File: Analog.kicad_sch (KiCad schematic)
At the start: 25 parts, among them Q2 2N7002, U3 74HC4051, U4 74HC4051, U5 OPA350, U6 MAX5423

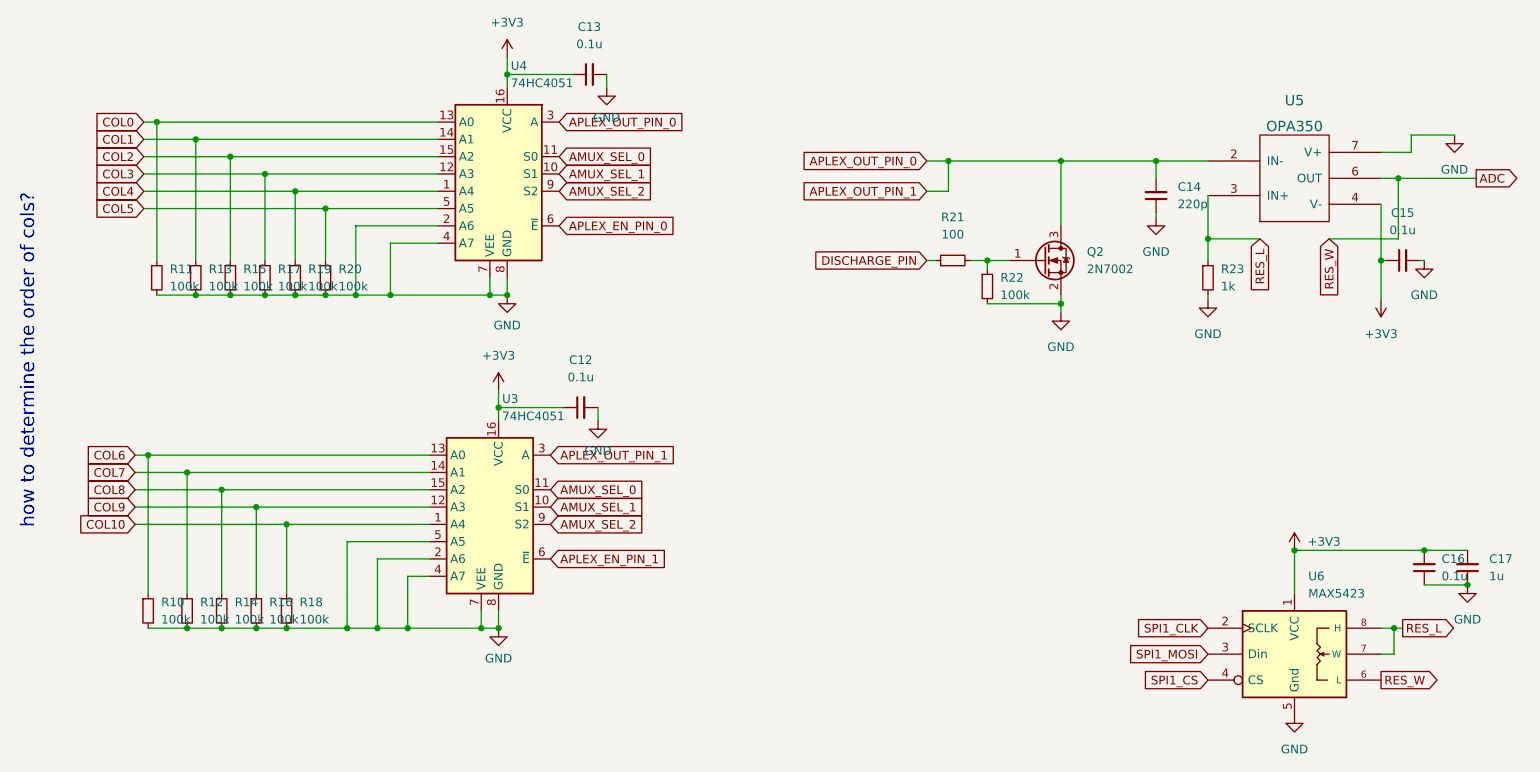
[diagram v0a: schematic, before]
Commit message: component placement
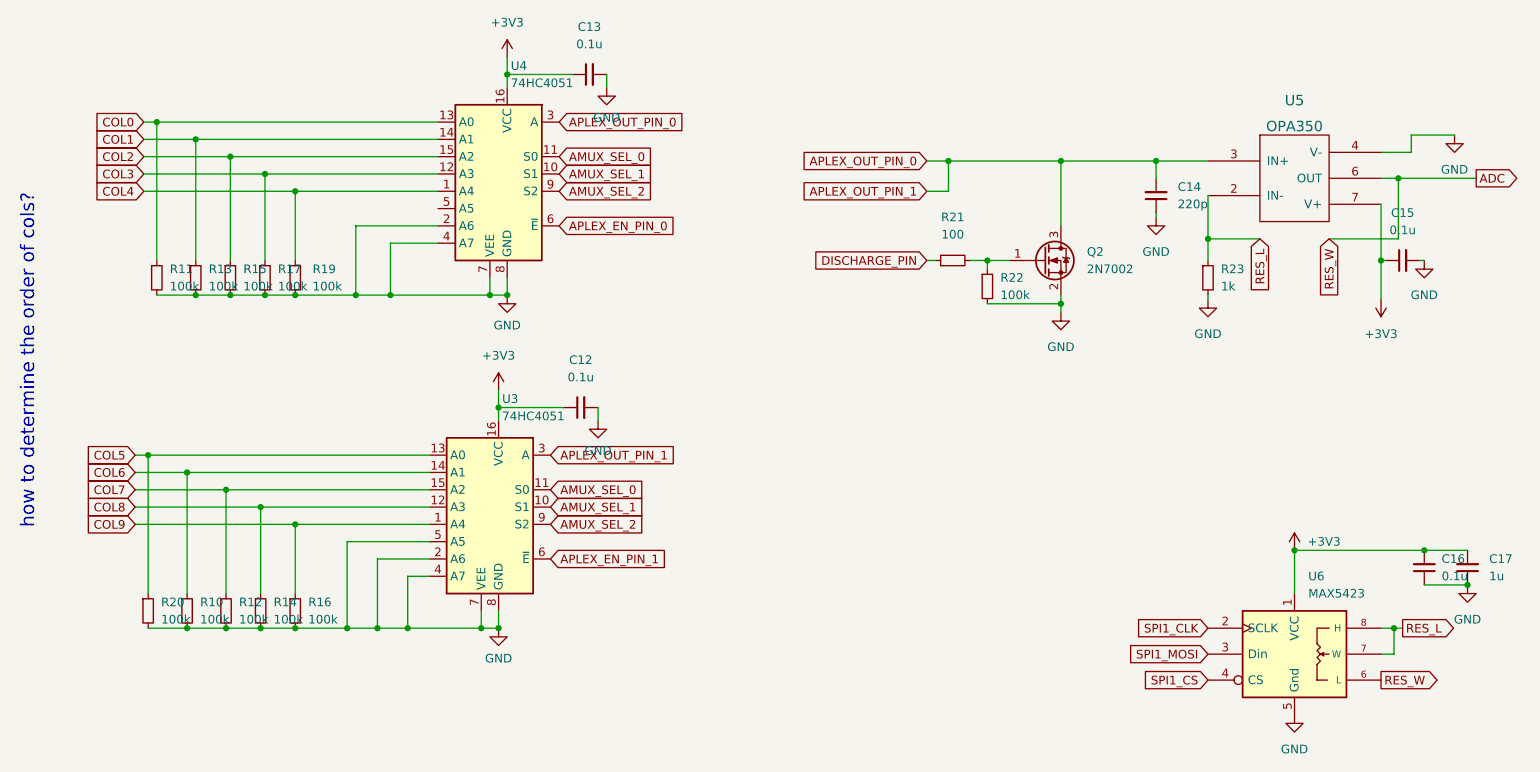
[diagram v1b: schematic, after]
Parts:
- removed R18: 100k, Resistor_SMD:R_0402_1005Metric, symbol Device:R_Small
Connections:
- net COL10 is gone; now on net COL9: U3.1 (A4)
- net +3V3: now also U5.7 (V+); no longer U5.4 (V-)
- net APLEX_OUT_PIN_0: now also U5.3 (IN+); no longer U5.2 (IN-)
- net COL5: now also U3.13 (A0); no longer U4.5 (A5)
- net COL6: now also U3.14 (A1); no longer U3.13 (A0)
- net COL7: now also U3.15 (A2); no longer U3.14 (A1)
- net COL8: now also U3.12 (A3); no longer U3.15 (A2)
- net COL9: no longer U3.12 (A3)
- net GND: now also U5.4 (V-); no longer U5.7 (V+)
- net RES_L: now also U5.2 (IN-); no longer U5.3 (IN+)
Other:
- moved on the sheet: R10, R12, R14, R16, R20

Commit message: routing work
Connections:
- net COL0: now also R15.1, U4.15 (A2); no longer R11.1, U4.13 (A0)
- net COL2: now also R11.1, U4.13 (A0); no longer R15.1, U4.15 (A2)
- net COL5: now also R12.1, U3.15 (A2); no longer R20.1, U3.13 (A0)
- net COL7: now also R20.1, U3.13 (A0); no longer R12.1, U3.15 (A2)
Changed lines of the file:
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@@
     )
   )
-  (global_label "COL2" (shape input) (at 67.945 47.625 180) (fields_autoplaced)
+  (global_label "COL2" (shape input) (at 67.945 42.545 180) (fields_autoplaced)
     (effects (font (size 1.27 1.27)) (justify right))
-    (property "Intersheet References" "${INTERSHEET_REFS}" (id 0) (at 60.6938 47.7044 0)
+    (property "Intersheet References" "${INTERSHEET_REFS}" (id 0) (at 60.6938 42.6244 0)
       (effects (font (size 1.27 1.27)) (justify right) hide)
     )
@@
     )
   )
-  (global_label "COL7" (shape input) (at 66.675 96.52 180) (fields_autoplaced)
+  (global_label "COL7" (shape input) (at 66.675 91.44 180) (fields_autoplaced)
     (effects (font (size 1.27 1.27)) (justify right))
-    (property "Intersheet References" "${INTERSHEET_REFS}" (id 0) (at 59.4238 96.5994 0)
+    (property "Intersheet References" "${INTERSHEET_REFS}" (id 0) (at 59.4238 91.5194 0)
       (effects (font (size 1.27 1.27)) (justify right) hide)
     )
@@
     )
   )
-  (global_label "COL0" (shape input) (at 67.945 42.545 180) (fields_autoplaced)
+  (global_label "COL0" (shape input) (at 67.945 47.625 180) (fields_autoplaced)
     (effects (font (size 1.27 1.27)) (justify right))
-    (property "Intersheet References" "${INTERSHEET_REFS}" (id 0) (at 60.6938 42.6244 0)
+    (property "Intersheet References" "${INTERSHEET_REFS}" (id 0) (at 60.6938 47.7044 0)
       (effects (font (size 1.27 1.27)) (justify right) hide)
     )
@@
     )
   )
-  (global_label "COL5" (shape input) (at 66.675 91.44 180) (fields_autoplaced)
+  (global_label "COL5" (shape input) (at 66.675 96.52 180) (fields_autoplaced)
     (effects (font (size 1.27 1.27)) (justify right))
-    (property "Intersheet References" "${INTERSHEET_REFS}" (id 0) (at 59.4238 91.5194 0)
+    (property "Intersheet References" "${INTERSHEET_REFS}" (id 0) (at 59.4238 96.5994 0)
       (effects (font (size 1.27 1.27)) (justify right) hide)
     )

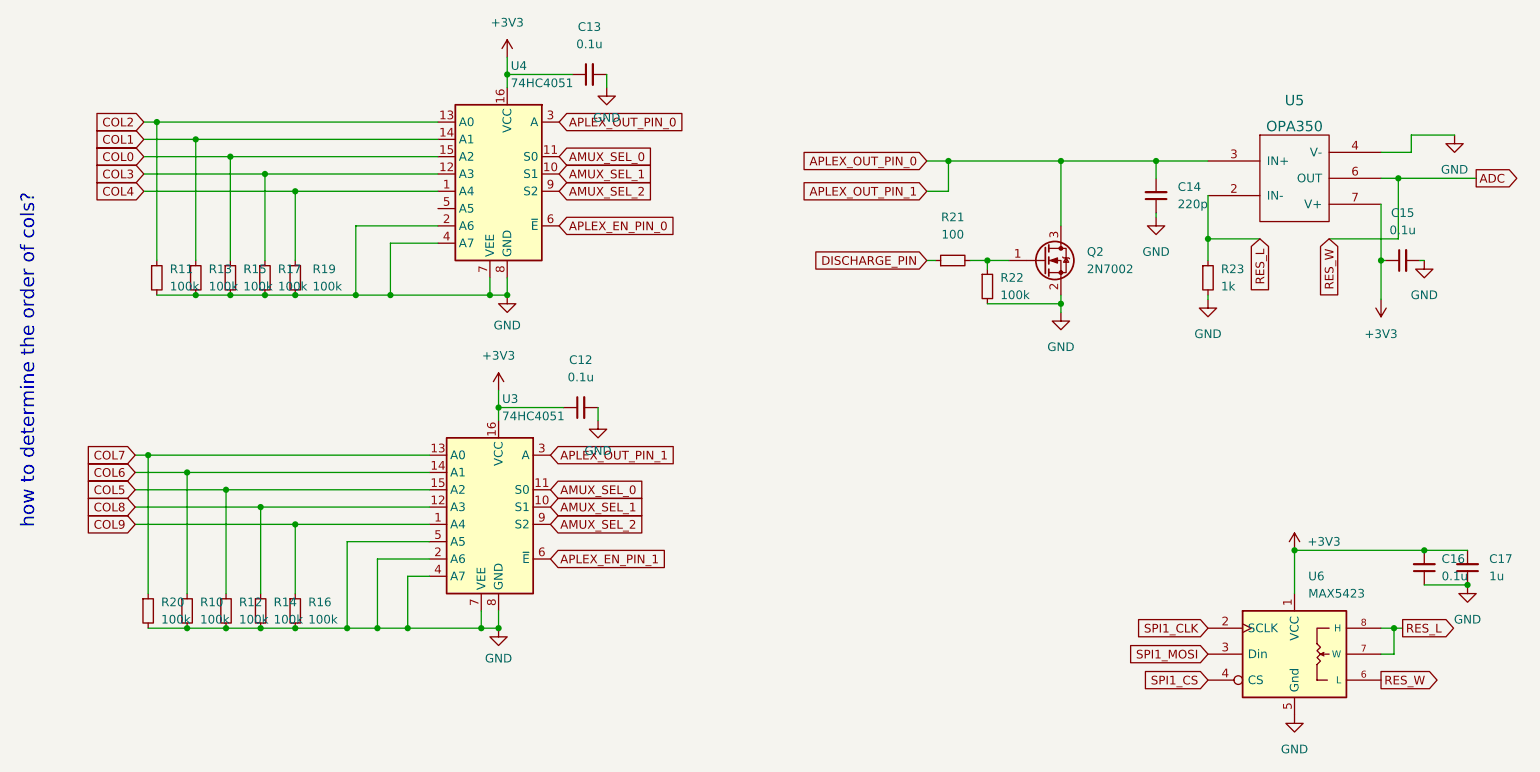
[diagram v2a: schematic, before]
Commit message: clean up folders, edit silkscreen
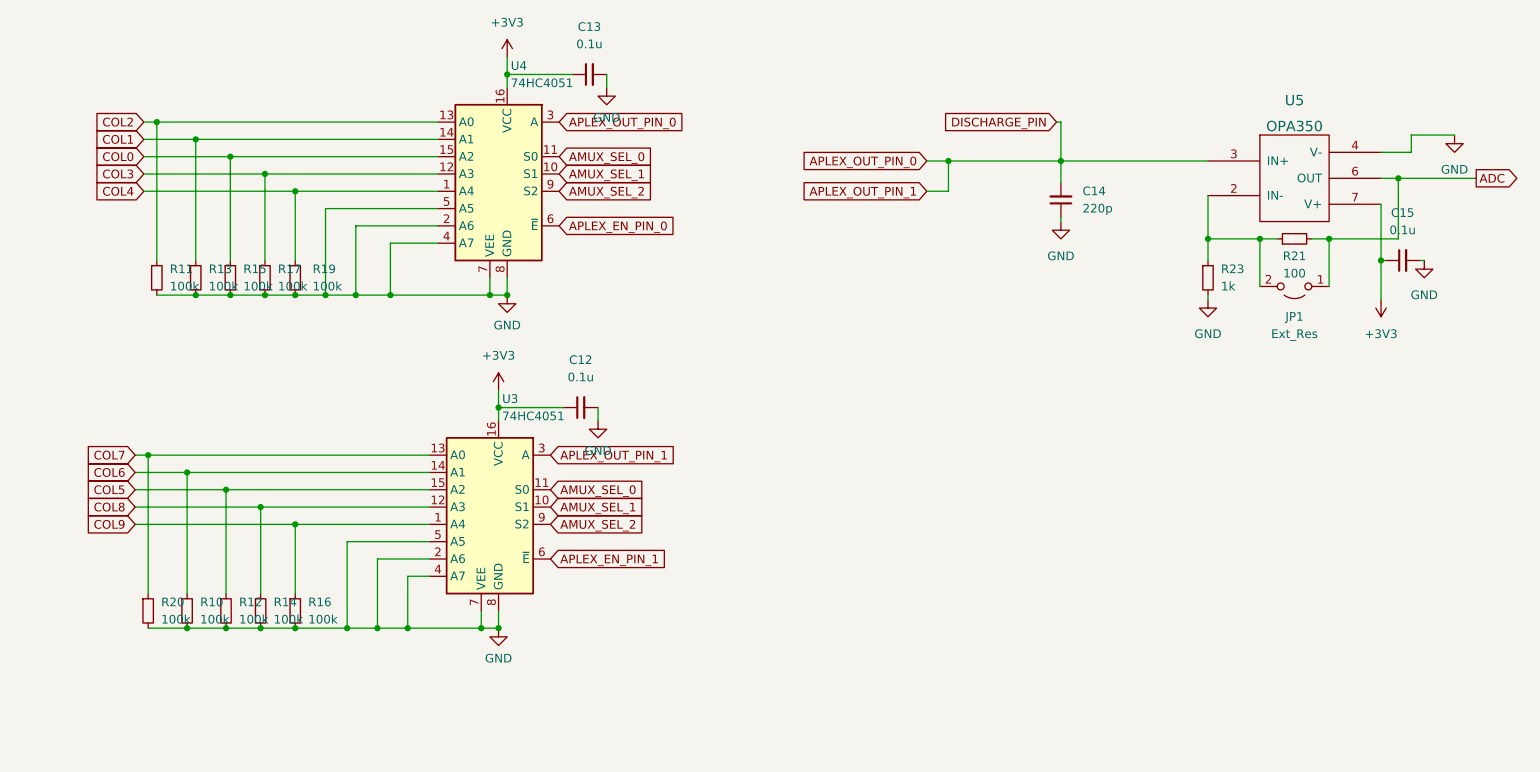
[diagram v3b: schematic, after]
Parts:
- removed C16: 0.1u, Capacitor_SMD:C_0402_1005Metric, symbol Device:C_Small
- removed C17: 1u, Capacitor_SMD:C_0402_1005Metric, symbol Device:C_Small
- removed Q2: 2N7002, Package_TO_SOT_SMD:SOT-23, symbol Transistor_FET:2N7002
- removed R22: 100k, Resistor_SMD:R_0402_1005Metric, symbol Device:R_Small
- removed U6: MAX5423, cipulot_parts:MAX5423, symbol cipulot_parts:MAX5423
- added JP1: Ext_Res, Resistor_SMD:R_0603_1608Metric_Pad0.98x0.95mm_HandSolder, symbol Jumper:Jumper_2_Open
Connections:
- net RES_L is gone; now on an unnamed net: R23.1, U5.2 (IN-)
- net ADC: now also R21.2, JP1.1 (A)
- net GND: now also U4.5 (A5)
- net DISCHARGE_PIN: no longer names the net of R21.1
- net DISCHARGE_PIN: now also JP1.2 (B)
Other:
- note removed: "how to determine the order of cols?"
- moved on the sheet: C14, R21
